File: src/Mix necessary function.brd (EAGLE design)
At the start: 53 x 58 mm, 22 parts, among them CON1 XT90PW-M, SW1 02-JST, SW2 02-JST

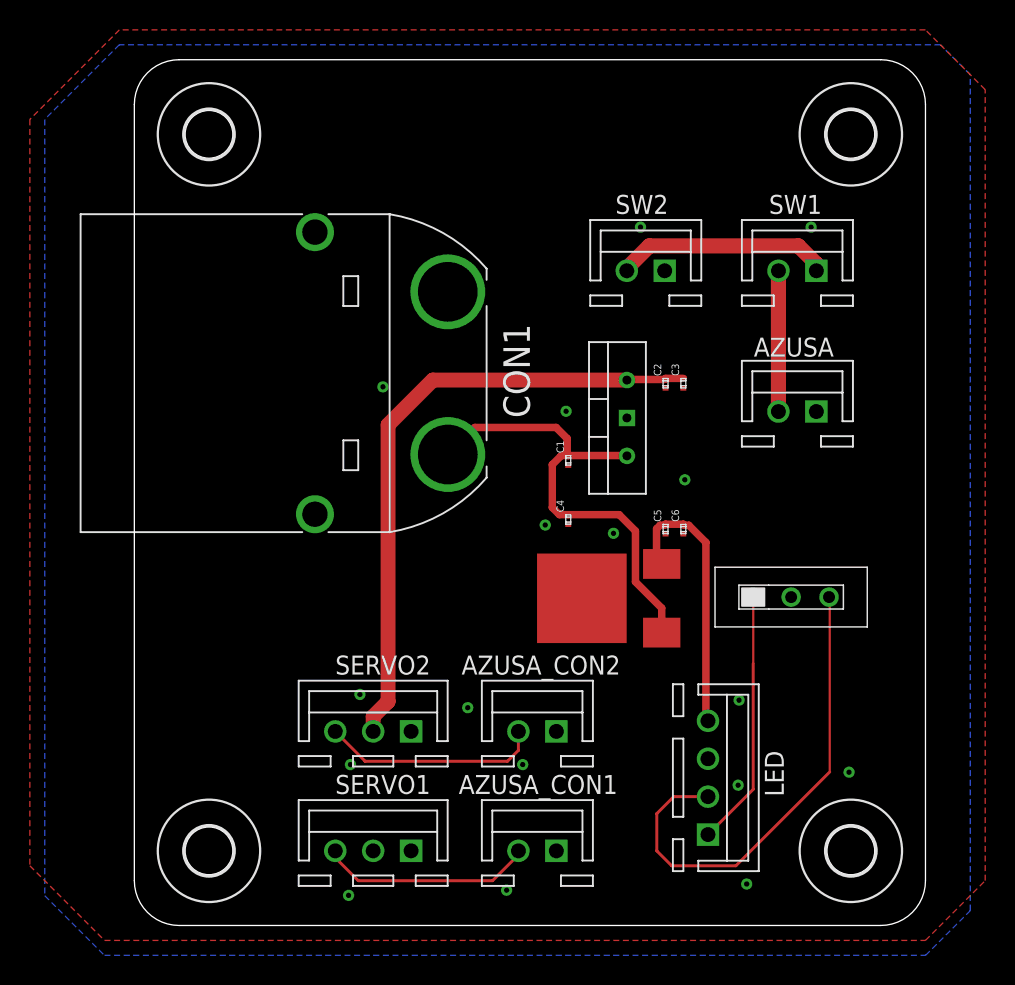
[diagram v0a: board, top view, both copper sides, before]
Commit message: fix twelite circuit slot
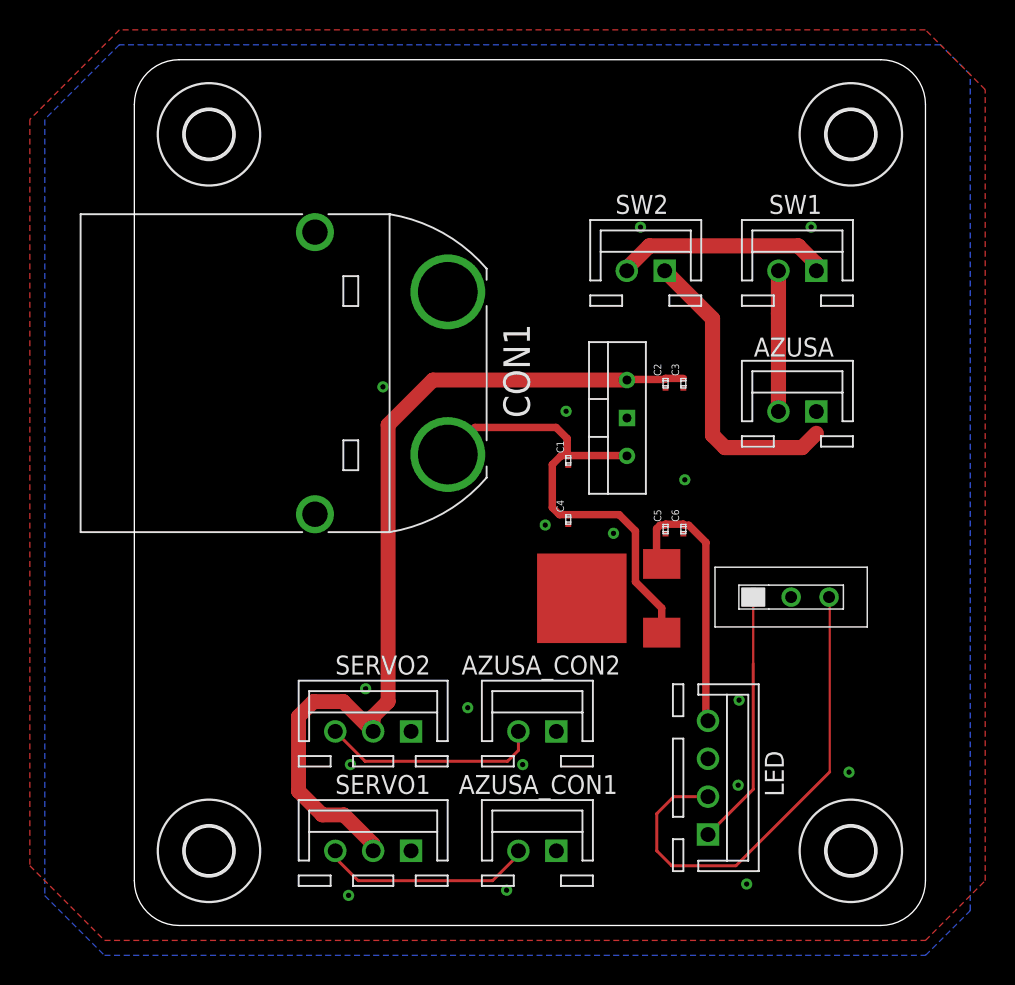
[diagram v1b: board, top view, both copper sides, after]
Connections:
- new net AGND: AZUSA.1, SW2.1
- net GND: no longer AZUSA.1, AZUSA_CON1.1, AZUSA_CON2.1, SW2.1
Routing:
- net AGND: track 0.00 -> 20.0 mm
- net +6V: track 42.0 -> 60.2 mm
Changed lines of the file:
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@@
 <drawing>
 <settings>
-<setting alwaysvectorfont="yes"/>
+<setting alwaysvectorfont="no"/>
 <setting verticaltext="up"/>
 </settings>
@@
 </signal>
 <signal name="GND">
-<contactref element="AZUSA" pad="1"/>
-<contactref element="SW2" pad="1"/>
 <contactref element="CON1" pad="-"/>
 <contactref element="C4" pad="2"/>
 <contactref element="U$17" pad="GND"/>
 <contactref element="C5" pad="2"/>
-<contactref element="AZUSA_CON1" pad="1"/>
 <contactref element="SERVO1" pad="1"/>
 <contactref element="C2" pad="2"/>
@@
 <contactref element="LED_SW" pad="C"/>
 <contactref element="SERVO2" pad="1"/>
-<contactref element="AZUSA_CON2" pad="1"/>
 <polygon width="0.2" layer="16">
 <vertex x="-1" y="50"/>
@@
 <vertex x="54" y="50"/>
 </polygon>
+<wire x1="36.778" y1="27.001" x2="35.587" y2="27.001" width="0" layer="19" extent="1-1"/>
+<wire x1="33" y1="25" x2="35.587" y2="27.001" width="0" layer="19" extent="1-1"/>
+<wire x1="29.068" y1="21.832" x2="33" y2="25" width="0" layer="19" extent="1-1"/>
+<wire x1="29.068" y1="17.871" x2="29.068" y2="21.832" width="0" layer="19" extent="1-1"/>
+<wire x1="29.98" y1="12.919" x2="29.068" y2="17.871" width="0" layer="19" extent="1-1"/>
+<wire x1="35.587" y1="17.233" x2="29.068" y2="17.871" width="0" layer="19" extent="1-1"/>
+<wire x1="36.778" y1="17.233" x2="35.587" y2="17.233" width="0" layer="19" extent="1-1"/>
+<wire x1="44" y1="13" x2="36.778" y2="17.233" width="0" layer="19" extent="1-1"/>
+<wire x1="21" y1="33.45" x2="29.068" y2="21.832" width="0" layer="19" extent="1-1"/>
+<wire x1="18.54" y1="4" x2="29.98" y2="12.919" width="0" layer="19" extent="1-1"/>
+<wire x1="18.54" y1="-4" x2="18.54" y2="4" width="0" layer="19" extent="1-1"/>
 </signal>
 <signal name="VCC">
 <contactref element="SW1" pad="2"/>
 <contactref element="AZUSA" pad="2"/>
-<wire x1="43.15" y1="25.43" x2="43.15" y2="34.86" width="1.016" layer="1"/>
+<wire x1="43.15" y1="25.43" x2="43.15" y2="32" width="1.016" layer="1"/>
+<wire x1="43.15" y1="32" x2="43.15" y2="34.86" width="1.016" layer="1"/>
 </signal>
 <signal name="EM">
@@
 <wire x1="16" y1="4" x2="16" y2="5" width="1" layer="1"/>
 <wire x1="16" y1="5" x2="17" y2="6" width="1" layer="1"/>
-<wire x1="16" y1="-4" x2="16" y2="4" width="0" layer="19" extent="1-1"/>
+<wire x1="16" y1="4" x2="14" y2="6" width="1" layer="1"/>
+<wire x1="14" y1="6" x2="12" y2="6" width="1" layer="1"/>
+<wire x1="12" y1="6" x2="11" y2="5" width="1" layer="1"/>
+<wire x1="11" y1="5" x2="11" y2="0" width="1" layer="1"/>
+<wire x1="11" y1="0" x2="12.5936" y2="-1.5936" width="1" layer="1"/>
+<wire x1="12.5936" y1="-1.5936" x2="14.04255" y2="-1.5936" width="1" layer="1"/>
+<wire x1="16" y1="-4" x2="16" y2="-3.55105" width="1" layer="1"/>
+<wire x1="16" y1="-3.55105" x2="14.04255" y2="-1.5936" width="1" layer="1"/>
 </signal>
 <signal name="RED">
@@
 <wire x1="13.46" y1="-4" x2="13.46" y2="-4.46" width="0.2" layer="1"/>
 <wire x1="13.46" y1="-4.46" x2="15" y2="-6" width="0.2" layer="1"/>
-<wire x1="15" y1="-6" x2="24" y2="-6" width="0.2" layer="1"/>
-<wire x1="24" y1="-6" x2="25.746" y2="-4.254" width="0.2" layer="1"/>
-<wire x1="25.746" y1="-4.254" x2="25.73" y2="-4" width="0" layer="19" extent="1-1"/>
+<wire x1="24" y1="-6" x2="15" y2="-6" width="0.2" layer="1"/>
+<wire x1="25.73" y1="-4" x2="25.73" y2="-4.27" width="0.2" layer="1"/>
+<wire x1="25.73" y1="-4.27" x2="24" y2="-6" width="0.2" layer="1"/>
 </signal>
 <signal name="N$1">
@@
 </signal>
 <signal name="N$4">
-<via x="15.113" y="6.477" extent="1-16" drill="0.35"/>
+<via x="15.494" y="6.858" extent="1-16" drill="0.35"/>
 </signal>
 <signal name="N$5">
@@
 <via x="45.339" y="37.782" extent="1-16" drill="0.35"/>
 </signal>
+<signal name="AGND">
+<contactref element="AZUSA" pad="1"/>
+<contactref element="SW2" pad="1"/>
+<wire x1="44.73586875" y1="23.0156" x2="39.56413125" y2="23.0156" width="1.016" layer="1"/>
+<wire x1="39.56413125" y1="23.0156" x2="38.7356" y2="23.84413125" width="1.016" layer="1"/>
+<wire x1="45.69" y1="23.96973125" x2="44.73586875" y2="23.0156" width="1.016" layer="1"/>
+<wire x1="38.7356" y1="31.6544" x2="35.53" y2="34.86" width="1.016" layer="1"/>
+<wire x1="38.7356" y1="23.84413125" x2="38.7356" y2="31.6544" width="1.016" layer="1"/>
+<wire x1="45.69" y1="23.96973125" x2="45.69" y2="25.43" width="0" layer="19" extent="1-1"/>
+</signal>
 </signals>

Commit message: add servo emergency
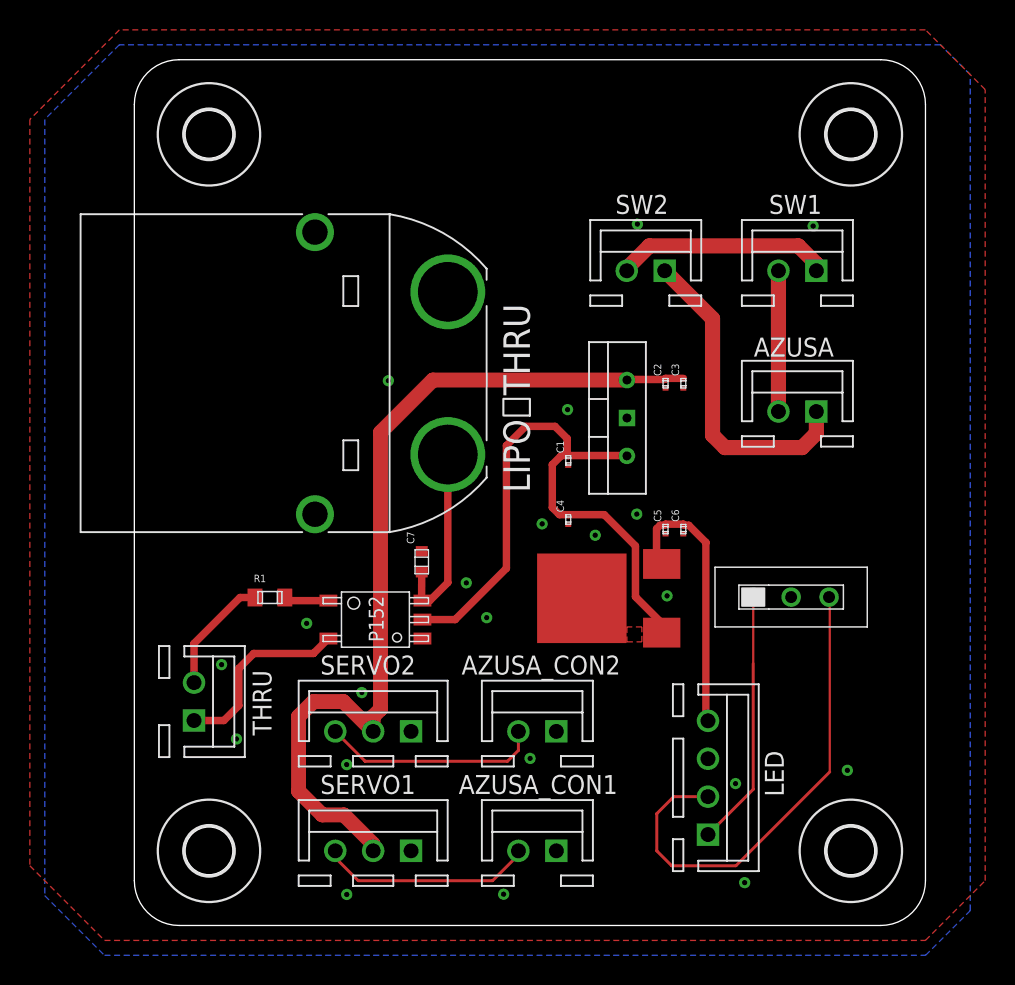
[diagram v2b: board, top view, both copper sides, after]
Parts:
- added C7: GCM188L81H104KA57, GCM188L81H104K57(0.1uF):GCM188L81H104KA57
- added R1: 100, CR0603:CR0603
- added THRU: 02-JST, con-jst-xh (1):B2B-XH
- added TLP1: TLP152, TLP152:TLP152
- renumbered CON1 to LIPO＿THRU
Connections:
- new net N$1: THRU.1, TLP1.CATHODE
- new net N$118: R1.RIGHT, TLP1.ANODE
- new net N$20: C7.P$1, LIPO＿THRU.+, TLP1.VCC
- new net N$92: R1.LEFT, THRU.2
- net GND: now also AZUSA_CON1.1, AZUSA_CON2.1, C7.P$2, TLP1.GND
- net PVCC: now also TLP1.VO; no longer LIPO＿THRU.+
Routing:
- net N$1: track 0.00 -> 12.7 mm, vias 1 -> 0
- net N$20: track 0.00 -> 12.7 mm
- net PVCC: track 32.1 -> 42.7 mm
- net N$92: track 0.00 -> 7.98 mm
- net N$118: track 0.00 -> 3.01 mm
- net AGND: track 20.0 -> 21.5 mm
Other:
- board text added: "R1"

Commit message: fix
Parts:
- added D1: GS2M-LTP, GS2M-LTP:GS2M-LTP
- added Q1: SQJA16EP-T1_GE3, SQJA16EP-T1_GE3:SQJA16EP-T1_GE3
- added R2: 820, CR0603:CR0603
- added R3: 10, CR0603:CR0603
- added R4: 10k, CR0603:CR0603
- added ZD1: MMBZ5248B-TP, MMBZ5248B-TP:MMBZ5248B-TP
- moved TLP1 7.00 mm to (6.00, 11.5)
- moved C7 6.86 mm to (12.4, 15.2)
- moved R1 5.39 mm to (4.03, 11.1), turned to 90 degrees
- moved THRU 1.00 mm to (4.00, 5.00)
- moved LED 0.72 mm to (39.0, 0.50)
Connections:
- new net N$6: D1.C, R2.LEFT, TLP1.VO
- new net N$7: Q1.G, R2.RIGHT, R3.RIGHT, R4.RIGHT, ZD1.CATHODE
- new net N$8: D1.A, R3.LEFT
- net N$20: now also Q1.D
- net PVCC: now also Q1.S1, Q1.S2, Q1.S3, R4.LEFT, ZD1.ANODE; no longer TLP1.VO
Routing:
- net N$7: track 0.00 -> 29.7 mm
- net PVCC: track 42.7 -> 69.4 mm, vias 0 -> 2
- net N$20: track 12.7 -> 32.1 mm
- net +6V: track 60.2 -> 70.8 mm
- net N$6: track 0.00 -> 6.09 mm
- net N$1: track 12.7 -> 8.13 mm
- net N$8: track 0.00 -> 4.49 mm
- net RED: track 32.7 -> 28.6 mm
- net N$92: track 7.98 -> 3.81 mm
- net PWM2_SERVO: track 14.7 -> 13.7 mm
- net N$118: track 3.01 -> 2.25 mm
- net +12V: track 18.4 -> 19.1 mm
- net BLUE: track 17.2 -> 17.8 mm
